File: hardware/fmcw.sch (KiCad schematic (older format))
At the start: 26 parts, among them U1 LP5907MFX-3.3, U2 LP5907MFX-1.8, U3 KT2520K-T, U4 NC7SVU04P5X, U5 NB3N551

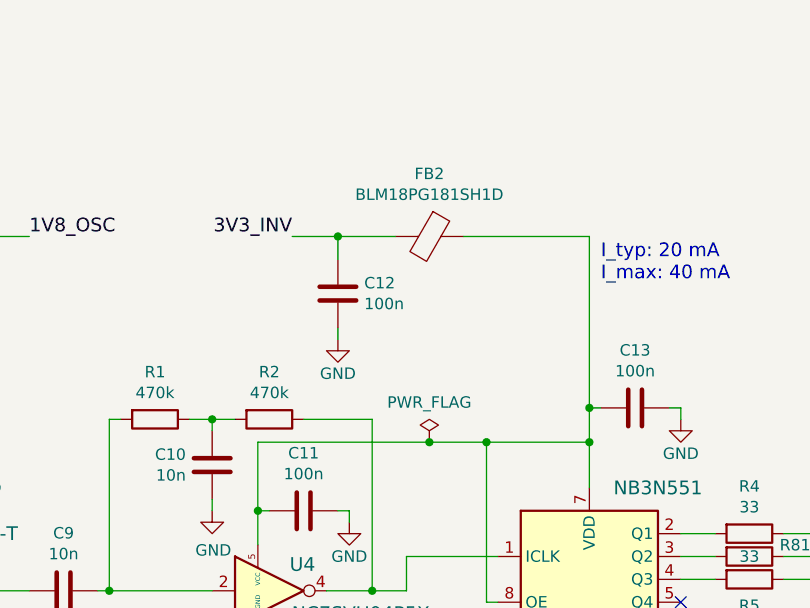
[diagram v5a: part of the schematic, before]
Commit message: Fixed transmission line width.
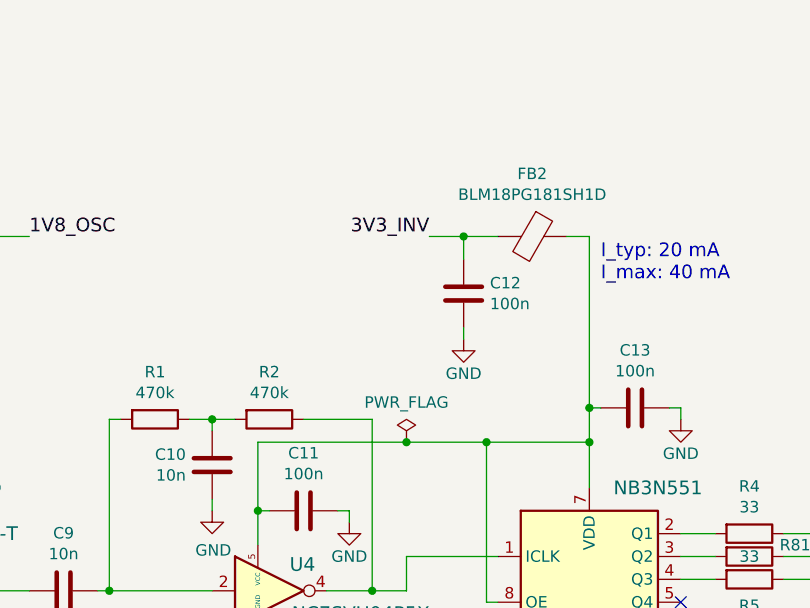
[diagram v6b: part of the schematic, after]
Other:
- moved on the sheet: C12, FB2
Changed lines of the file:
@@
 L Device:Ferrite_Bead FB2
 U 1 1 5973E6F9
-P 4450 5300
-F 0 "FB2" V 4176 5300 50  0000 C CNN
-F 1 "BLM18PG181SH1D" V 4267 5300 50  0000 C CNN
-F 2 "Inductor_SMD:L_0603_1608Metric" H 4450 5300 60  0001 C CNN
-F 3 "https://www.murata.com/en-us/products/productdata/8796738650142/ENFA0003.pdf" H 4450 5300 60  0001 C CNN
-F 4 "BLM18PG181SH1D" H 100 0   50  0001 C CNN "MFN"
-	1    4450 5300
+P 4900 5300
+F 0 "FB2" V 4626 5300 50  0000 C CNN
+F 1 "BLM18PG181SH1D" V 4717 5300 50  0000 C CNN
+F 2 "Inductor_SMD:L_0603_1608Metric" H 4900 5300 60  0001 C CNN
+F 3 "https://www.murata.com/en-us/products/productdata/8796738650142/ENFA0003.pdf" H 4900 5300 60  0001 C CNN
+F 4 "BLM18PG181SH1D" H 550 0   50  0001 C CNN "MFN"
+	1    4900 5300
 	0    1    1    0
 $EndComp
@@
 	1350 5300 1400 5300
 Wire Wire Line
-	4700 6200 4450 6200
-Wire Wire Line
 	5150 7250 5150 7300
 Wire Wire Line
@@
 Wire Wire Line
 	5550 6800 5700 6800
-Wire Wire Line
-	3850 5300 4050 5300
 Text Notes 1650 1550 0    60   ~ 0
 Quiescent current\n1V0:  97 mA\n1V8:  22 mA\n3V3D: 71 mA\n3V6:  78 mA
@@
 Text Label 7800 4650 0    60   ~ 0
 3V3D
-Text Label 3850 5300 2    60   ~ 0
+Text Label 4450 5300 2    60   ~ 0
 3V3_INV
 $Comp
 L power:PWR_FLAG #FLG02
 U 1 1 5CE75A5A
-P 4450 6200
-F 0 "#FLG02" H 4450 6275 50  0001 C CNN
-F 1 "PWR_FLAG" H 4450 6374 50  0000 C CNN
-F 2 "" H 4450 6200 50  0001 C CNN
-F 3 "~" H 4450 6200 50  0001 C CNN
-	1    4450 6200
+P 4350 6200
+F 0 "#FLG02" H 4350 6275 50  0001 C CNN
+F 1 "PWR_FLAG" H 4350 6374 50  0000 C CNN
+F 2 "" H 4350 6200 50  0001 C CNN
+F 3 "~" H 4350 6200 50  0001 C CNN
+	1    4350 6200
 	1    0    0    -1
 $EndComp
@@
 L Device:C C12
 U 1 1 5D4C5601
-P 4050 5550
-F 0 "C12" H 4165 5596 50  0000 L CNN
-F 1 "100n" H 4165 5505 50  0000 L CNN
-F 2 "Capacitor_SMD:C_0402_1005Metric" H 4088 5400 30  0001 C CNN
-F 3 "" H 4050 5550 60  0000 C CNN
-F 4 "CL05B104KO5NNNC" H -750 0   50  0001 C CNN "MFN"
-	1    4050 5550
-	1    0    0    -1
-$EndComp
-Wire Wire Line
-	4050 5400 4050 5300
-Connection ~ 4050 5300
-Wire Wire Line
-	4050 5300 4300 5300
+P 4600 5550
+F 0 "C12" H 4715 5596 50  0000 L CNN
+F 1 "100n" H 4715 5505 50  0000 L CNN
+F 2 "Capacitor_SMD:C_0402_1005Metric" H 4638 5400 30  0001 C CNN
+F 3 "" H 4600 5550 60  0000 C CNN
+F 4 "CL05B104KO5NNNC" H -200 0   50  0001 C CNN "MFN"
+	1    4600 5550
+	1    0    0    -1
+$EndComp
+Wire Wire Line
+	4600 5400 4600 5300
 $Comp
 L power:GND #PWR016
 U 1 1 5D4CBADA
-P 4050 5750
-F 0 "#PWR016" H 4050 5500 50  0001 C CNN
-F 1 "GND" H 4050 5600 50  0000 C CNN
-F 2 "" H 4050 5750 60  0000 C CNN
-F 3 "" H 4050 5750 60  0000 C CNN
-	1    4050 5750
-	1    0    0    -1
-$EndComp
-Wire Wire Line
-	4050 5750 4050 5700
+P 4600 5750
+F 0 "#PWR016" H 4600 5500 50  0001 C CNN
+F 1 "GND" H 4600 5600 50  0000 C CNN
+F 2 "" H 4600 5750 60  0000 C CNN
+F 3 "" H 4600 5750 60  0000 C CNN
+	1    4600 5750
+	1    0    0    -1
+$EndComp
+Wire Wire Line
+	4600 5750 4600 5700
 Wire Wire Line
 	5550 6700 5700 6700
@@
 Wire Wire Line
 	4700 6200 5150 6200
-Connection ~ 4450 6200
-Wire Wire Line
-	3700 6200 4450 6200
+Wire Wire Line
+	3700 6200 4350 6200
 $Comp
 L Device:R R81
@@
 	5200 6050 5150 6050
 Wire Wire Line
-	4600 5300 5150 5300
+	5050 5300 5150 5300
 Connection ~ 5150 6050
 Wire Wire Line
@@
 	1    0    0    -1
 $EndComp
+Connection ~ 4600 5300
+Wire Wire Line
+	4600 5300 4750 5300
+Wire Wire Line
+	4450 5300 4600 5300
+Connection ~ 4350 6200
+Wire Wire Line
+	4350 6200 4700 6200
 $EndSCHEMATC

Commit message: Finish FPGA code.
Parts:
- C1, C2, C3, C5: MFN CL21B106KQQNNNE -> ‎CL21B106KOQNNNE‎
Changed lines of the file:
@@
 F3 "MUXOUT" O L 8800 2500 60
 F4 "ADF_CE" I L 8800 2300 60
-F5 "ADC_TXDATA" I L 8800 2800 60
-F6 "ADC_CLK" I L 8800 2600 60
-F7 "ADC_DATA" I L 8800 2700 60
+F5 "ADF_TXDATA" I L 8800 2800 60
+F6 "ADF_CLK" I L 8800 2600 60
+F7 "ADF_DATA" I L 8800 2700 60
 F8 "ADF_LE" I L 8800 2400 60
 F9 "10V" I L 8800 1950 60
@@
 ADC_VCM2
 Text Label 3300 1850 0    60   ~ 0
-ADC_CE
+ADF_CE
 Text Label 3300 1950 0    60   ~ 0
 ADF_LE
@@
 MIX_ENBL
 Text Label 8700 2300 2    60   ~ 0
-ADC_CE
+ADF_CE
 Text Label 8700 2400 2    60   ~ 0
 ADF_LE
@@
 F 2 "Capacitor_SMD:C_0805_2012Metric" H 1088 4050 30  0001 C CNN
 F 3 "" H 1050 4200 60  0000 C CNN
-F 4 "CL21B106KQQNNNE" H -7800 -2450 50  0001 C CNN "MFN"
+F 4 "‎CL21B106KOQNNNE‎" H -7800 -2450 50  0001 C CNN "MFN"
 	1    1050 4200
 	1    0    0    -1
@@
 F 2 "Capacitor_SMD:C_0805_2012Metric" H 2188 4050 30  0001 C CNN
 F 3 "" H 2150 4200 60  0000 C CNN
-F 4 "CL21B106KQQNNNE" H -8100 -2650 50  0001 C CNN "MFN"
+F 4 "‎CL21B106KOQNNNE‎" H -8100 -2650 50  0001 C CNN "MFN"
 	1    2150 4200
 	1    0    0    -1
@@
 F 2 "Capacitor_SMD:C_0805_2012Metric" H 1138 5350 30  0001 C CNN
 F 3 "" H 1100 5500 60  0000 C CNN
-F 4 "CL21B106KQQNNNE" H -7750 -1150 50  0001 C CNN "MFN"
+F 4 "‎CL21B106KOQNNNE‎" H -7750 -1150 50  0001 C CNN "MFN"
 	1    1100 5500
 	1    0    0    -1
@@
 F 2 "Capacitor_SMD:C_0805_2012Metric" H 2188 5350 30  0001 C CNN
 F 3 "" H 2150 5500 60  0000 C CNN
-F 4 "CL21B106KQQNNNE" H -6700 -1150 50  0001 C CNN "MFN"
+F 4 "‎CL21B106KOQNNNE‎" H -6700 -1150 50  0001 C CNN "MFN"
 	1    2150 5500
 	1    0    0    -1
